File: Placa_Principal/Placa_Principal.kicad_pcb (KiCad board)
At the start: 2 copper layers, 126.7 x 163.3 mm, 23 parts, among them J1 Conn_01x02, J2 Conn_01x02, J3 Conn_01x02, J4 Conn_01x02, J5 Conn_01x02, Q1 BC547, Q2 IRF9540N, SW1 MTS102-C4, U1 LM358, U2 ESP32-S3-DevKitC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

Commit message: Segundo commit
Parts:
- added C2: 100uF, Capacitor_THT:CP_Radial_D8.0mm_P3.50mm, F.Cu at (53.9, 85.6)
- added R5: 330, Resistor_THT:R_Axial_DIN0204_L3.6mm_D1.6mm_P5.08mm_Horizontal, F.Cu at (70.4, 146.4)
- added U7: 4N25, Package_DIP:DIP-8_W7.62mm_Socket, F.Cu at (67.2, 121.8)
- D1: footprint LED_THT:LED_D4.0mm -> LED_THT:LED_D10.0mm
- moved J2 35.7 mm to (99.3, 84.9), turned to 180 degrees
- moved Q2 30.3 mm to (131.1, 153.7)
- moved J3 21.7 mm to (92.2, 84.9), turned to 180 degrees
- moved J1 20.0 mm to (106.9, 157.9)
- moved R4 17.6 mm to (95.4, 124.6)
- moved D1 13.3 mm to (96.4, 135.5)
- moved SW1 12.7 mm to (81.3, 162.2)
- moved J5 9.07 mm to (77.9, 84.9), turned to 180 degrees
- moved J4 8.54 mm to (85.0, 84.9), turned to 180 degrees
- moved U4 6.58 mm to (136.2, 71.9), turned to 0 degrees
- moved U3 4.14 mm to (88.6, 143.3), turned to 90 degrees
- moved U6 3.22 mm to (110.3, 73.0)
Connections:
- J2 pad 1: Net-(J2-Pin_1) -> ESP_GPIO04
- J2 pad 2: Net-(J2-Pin_2) -> ESP_GPIO05
- J3 pad 1: Net-(J3-Pin_1) -> ESP_GPIO06
- J3 pad 2: Net-(J3-Pin_2) -> ESP_GPIO07
- J4 pad 1: Net-(J4-Pin_1) -> ESP_GPIO15
- J4 pad 2: Net-(J4-Pin_2) -> ESP_GPIO16
- J5 pad 1: Net-(J5-Pin_1) -> ESP_GPIO17
- J5 pad 2: Net-(J5-Pin_2) -> ESP_GPIO18
- U2 pad 10: unconnected-(U2-GPIO17/ADC2_CH6-Pad10) -> ESP_GPIO17
- U2 pad 11: unconnected-(U2-GPIO18/ADC2_CH7-Pad11) -> ESP_GPIO18
- U2 pad 12: unconnected-(U2-GPIO8/ADC1_CH7-Pad12) -> ESP_GPIO08
- U2 pad 13: unconnected-(U2-GPIO3/ADC1_CH2-Pad13) -> ESP_GPIO03
- U2 pad 14: unconnected-(U2-GPIO46-Pad14) -> ESP_GPIO46
- U2 pad 15: unconnected-(U2-GPIO9/ADC1_CH8-Pad15) -> ESP_GPIO09
- U2 pad 16: unconnected-(U2-GPIO10/ADC1_CH9-Pad16) -> SPI
- U2 pad 17: unconnected-(U2-GPIO11/ADC2_CH0-Pad17) -> SPI
- U2 pad 18: unconnected-(U2-GPIO12/ADC2_CH1-Pad18) -> SPI
- U2 pad 19: unconnected-(U2-GPIO13/ADC2_CH2-Pad19) -> SPI
- U2 pad 20: unconnected-(U2-GPIO14/ADC2_CH3-Pad20) -> ESP_GPIO14
- U2 pad 30: unconnected-(U2-GPIO45-Pad30) -> ESP_GPIO45
- U2 pad 4: unconnected-(U2-GPIO4/ADC1_CH3-Pad4) -> ESP_GPIO04
- U2 pad 5: unconnected-(U2-GPIO5/ADC1_CH4-Pad5) -> ESP_GPIO05
- U2 pad 6: unconnected-(U2-GPIO6/ADC1_CH5-Pad6) -> ESP_GPIO06
- U2 pad 7: unconnected-(U2-GPIO7/ADC1_CH6-Pad7) -> ESP_GPIO07
- U2 pad 8: unconnected-(U2-GPIO15/ADC2_CH4/32K_P-Pad8) -> ESP_GPIO15
- U2 pad 9: unconnected-(U2-GPIO16/ADC2_CH5/32K_N-Pad9) -> ESP_GPIO16
- U4 pad 1: Net-(J3-Pin_2) -> unconnected-(U4-IN1L-Pad1)
- U4 pad 2: Net-(J3-Pin_1) -> unconnected-(U4-IN2L-Pad2)
- U4 pad 3: Net-(J2-Pin_2) -> unconnected-(U4-IN3L-Pad3)
- U4 pad 4: Net-(J2-Pin_1) -> unconnected-(U4-IN4L-Pad4)
- U5 pad 1: Net-(J5-Pin_2) -> unconnected-(U5-IN1L-Pad1)
- U5 pad 2: Net-(J5-Pin_1) -> unconnected-(U5-IN2L-Pad2)
- U5 pad 3: Net-(J4-Pin_2) -> unconnected-(U5-IN3L-Pad3)
- U5 pad 4: Net-(J4-Pin_1) -> unconnected-(U5-IN4L-Pad4)
- U6 pad 1: unconnected-(U6-VCC-Pad1) -> +3.3V
- U6 pad 2: unconnected-(U6-GND-Pad2) -> GND
- U6 pad 3: unconnected-(U6-SCL/SCLK-Pad3) -> ESP_GPIO09
- U6 pad 4: unconnected-(U6-SDA/SDI-Pad4) -> ESP_GPIO08
- U6 pad 7: unconnected-(U6-AD0/SDO-Pad7) -> ESP_GPIO46
- U6 pad 8: unconnected-(U6-INT-Pad8) -> ESP_GPIO03
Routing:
- net VCC: track 0.00 -> 48.5 mm
- net GND: track 63.4 -> 111.9 mm

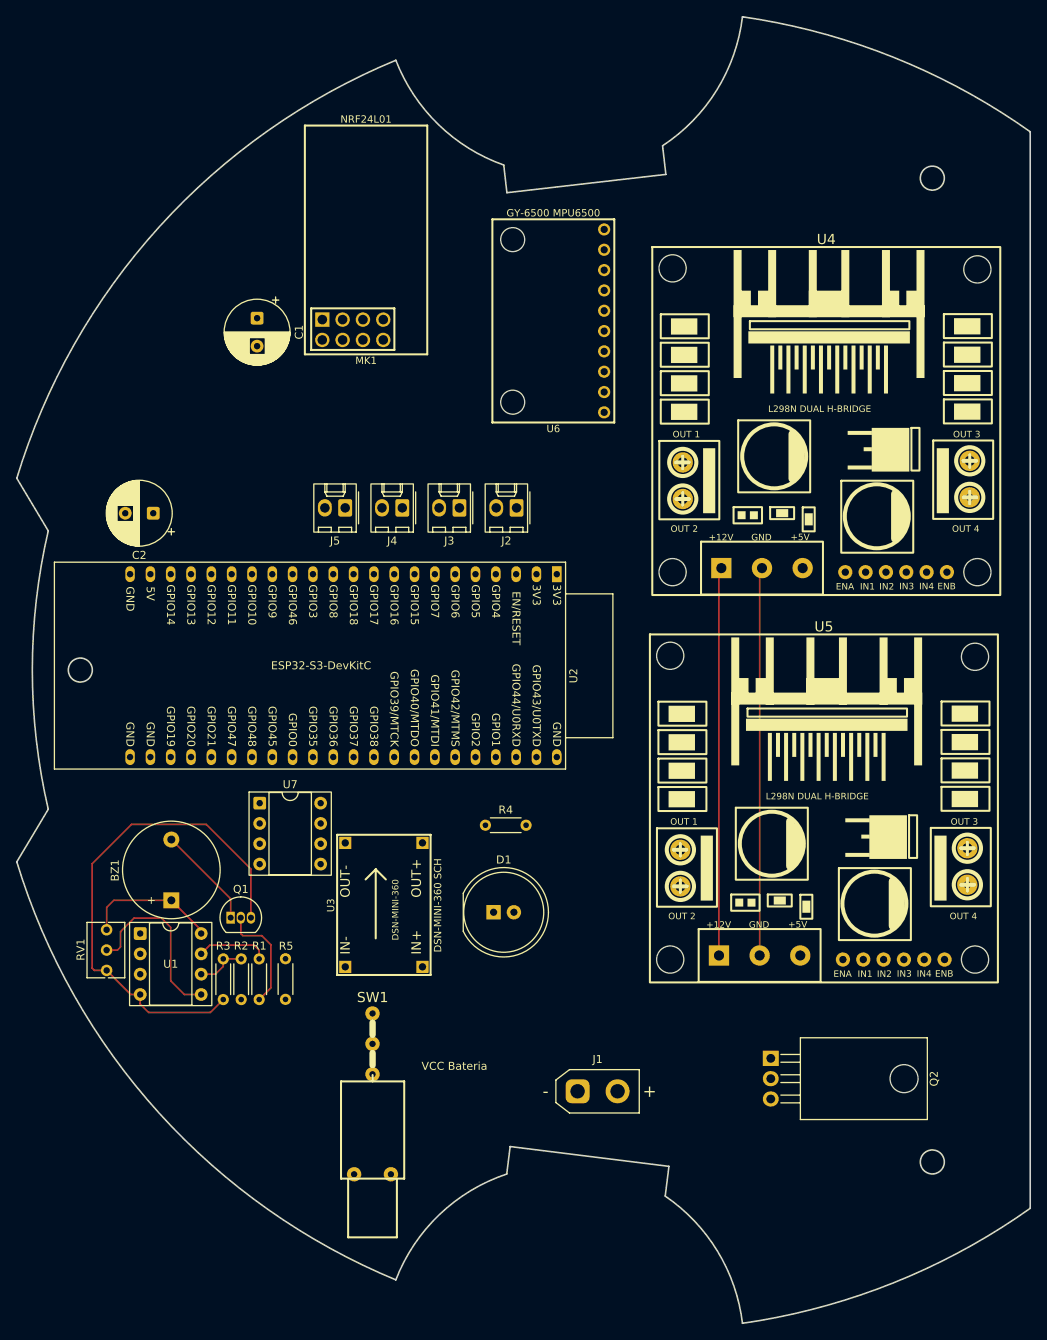
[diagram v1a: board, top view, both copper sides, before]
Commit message: Finalizando o esquemático e rearranjando a posição dos componentes na PCB
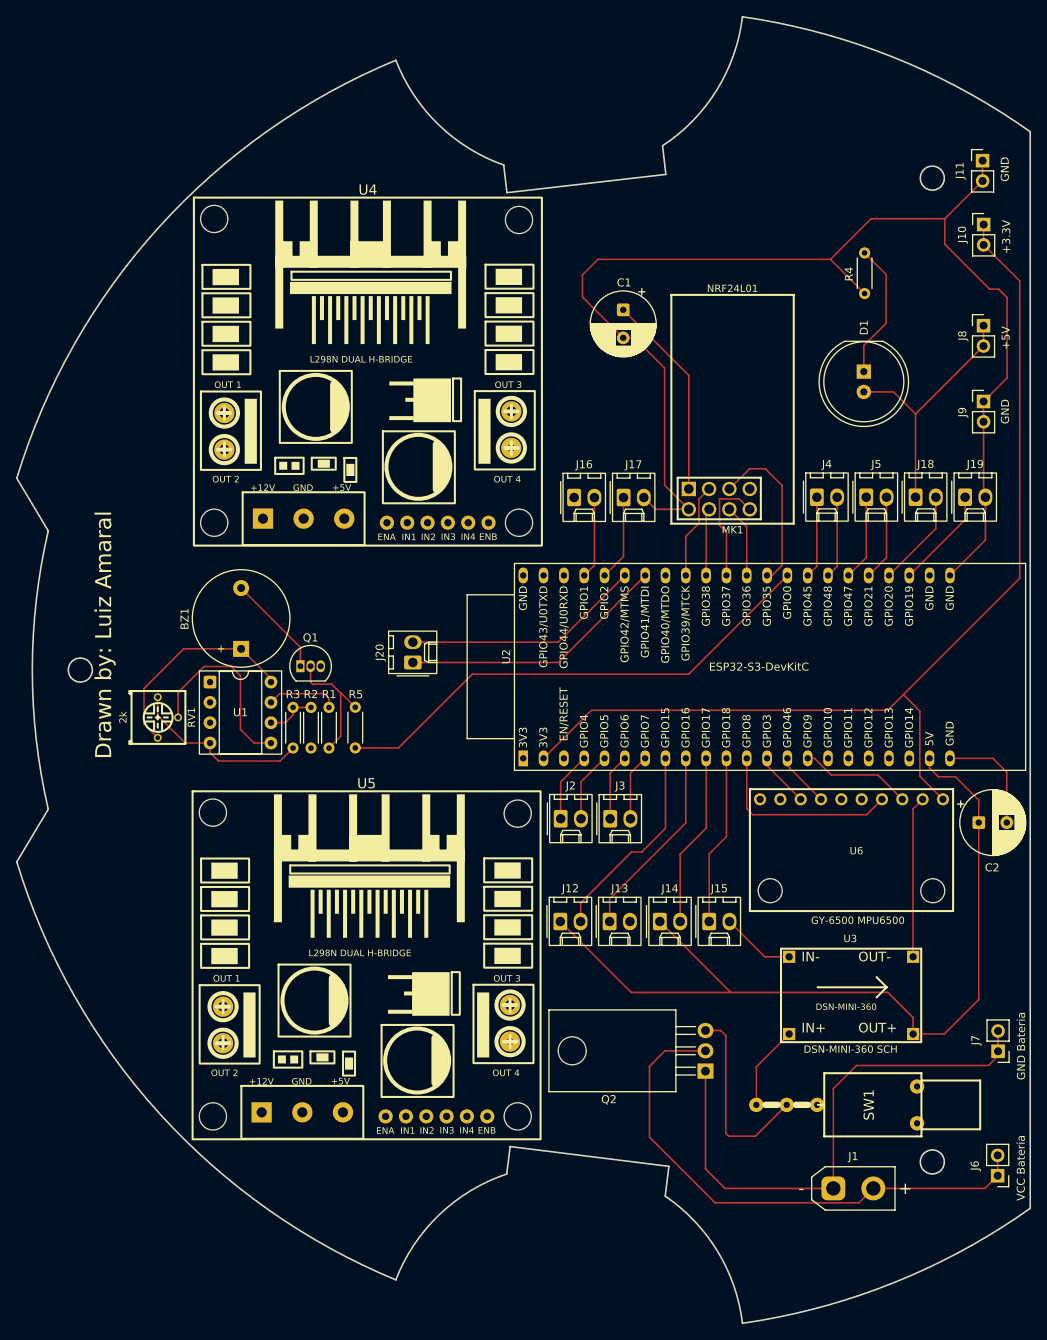
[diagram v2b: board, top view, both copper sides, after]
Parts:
- removed U7: 4N25, Package_DIP:DIP-8_W7.62mm_Socket
- added J10: Conn_01x02_Pin, Connector_PinHeader_2.54mm:PinHeader_1x02_P2.54mm_Vertical, F.Cu at (157.7, 49.5)
- added J11: Conn_01x02_Pin, Connector_PinHeader_2.54mm:PinHeader_1x02_P2.54mm_Vertical, F.Cu at (157.6, 41.5)
- added J12: Conn_01x02, Connector_Molex:Molex_KK-254_AE-6410-02A_1x02_P2.54mm_Vertical, F.Cu at (104.8, 136.6)
- added J13: Conn_01x02, Connector_Molex:Molex_KK-254_AE-6410-02A_1x02_P2.54mm_Vertical, F.Cu at (110.9, 136.6)
- added J14: Conn_01x02, Connector_Molex:Molex_KK-254_AE-6410-02A_1x02_P2.54mm_Vertical, F.Cu at (117.2, 136.6)
- added J15: Conn_01x02, Connector_Molex:Molex_KK-254_AE-6410-02A_1x02_P2.54mm_Vertical, F.Cu at (123.4, 136.6)
- added J16: Conn_01x02, Connector_Molex:Molex_KK-254_AE-6410-02A_1x02_P2.54mm_Vertical, F.Cu at (106.5, 83.6)
- added J17: Conn_01x02, Connector_Molex:Molex_KK-254_AE-6410-02A_1x02_P2.54mm_Vertical, F.Cu at (112.7, 83.6)
- added J18: Conn_01x02, Connector_Molex:Molex_KK-254_AE-6410-02A_1x02_P2.54mm_Vertical, F.Cu at (149.2, 83.6)
- added J19: Conn_01x02, Connector_Molex:Molex_KK-254_AE-6410-02A_1x02_P2.54mm_Vertical, F.Cu at (155.4, 83.6)
- added J20: Conn_01x02, Connector_Molex:Molex_KK-254_AE-6410-02A_1x02_P2.54mm_Vertical, F.Cu at (86.3, 104.3)
- added J6: Conn_01x02_Pin, Connector_PinHeader_2.54mm:PinHeader_1x02_P2.54mm_Vertical, F.Cu at (159.4, 168.4)
- added J7: Conn_01x02_Pin, Connector_PinHeader_2.54mm:PinHeader_1x02_P2.54mm_Vertical, F.Cu at (159.5, 152.9)
- added J8: Conn_01x02_Pin, Connector_PinHeader_2.54mm:PinHeader_1x02_P2.54mm_Vertical, F.Cu at (157.7, 62.2)
- added J9: Conn_01x02_Pin, Connector_PinHeader_2.54mm:PinHeader_1x02_P2.54mm_Vertical, F.Cu at (157.7, 71.6)
- R5: value 330 -> ?
- RV1: value R_Potentiometer -> 2k; footprint Potentiometer_THT:Potentiometer_Bourns_3266Y_Vertical -> Custom_Footprints:RTRIM3362P
- moved C2 110.2 mm to (157.1, 124.3), turned to 0 degrees
- moved R4 85.8 mm to (142.8, 53.1), turned to -90 degrees
- moved D1 81.9 mm to (142.7, 67.9), turned to -90 degrees
- moved J5 65.1 mm to (143.0, 83.6), turned to 0 degrees
- moved U6 64.3 mm to (152.6, 121.4), turned to -90 degrees
- moved SW1 62.1 mm to (143.4, 159.6), turned to 90 degrees
- moved U5 60.4 mm to (78.8, 139.9)
- moved U4 57.6 mm to (78.9, 65.7)
- moved J4 51.8 mm to (136.8, 83.6), turned to 0 degrees
- moved MK1 50.5 mm to (124.7, 83.8)
- moved C1 45.8 mm to (112.6, 60.2)
- moved U3 44.6 mm to (132.4, 151.7), turned to 0 degrees
- moved J3 43.2 mm to (111.0, 123.8), turned to 0 degrees
- moved J2 39.3 mm to (104.8, 123.8), turned to 0 degrees
- moved J1 34.2 mm to (138.9, 170.0)
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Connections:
- J4 pad 1: ESP_GPIO15 -> ESP_GPIO45
- J4 pad 2: ESP_GPIO16 -> ESP_GPIO48
- J5 pad 1: ESP_GPIO17 -> ESP_GPIO47
- J5 pad 2: ESP_GPIO18 -> ESP_GPIO21
- R5 pad 1: ESP_GPIO14 -> ESP_GPIO00
- U2 pad 16: SPI -> SPI_CS
- U2 pad 17: SPI -> SPI_MOSI
- U2 pad 18: SPI -> SPI_CLK
- U2 pad 19: SPI -> SPI_MISO
- U2 pad 20: ESP_GPIO14 -> unconnected-(U2-GPIO14/ADC2_CH3-Pad20)
- U2 pad 25: unconnected-(U2-GPIO19/USB_D--Pad25) -> ESP_GPIO19
- U2 pad 26: unconnected-(U2-GPIO20/USB_D+-Pad26) -> ESP_GPIO20
- U2 pad 27: unconnected-(U2-GPIO21-Pad27) -> ESP_GPIO21
- U2 pad 28: unconnected-(U2-GPIO47-Pad28) -> ESP_GPIO47
- U2 pad 29: unconnected-(U2-GPIO48-Pad29) -> ESP_GPIO48
- U2 pad 31: unconnected-(U2-GPIO0-Pad31) -> ESP_GPIO00
- U2 pad 38: unconnected-(U2-GPIO41/MTDI-Pad38) -> ESP_GPIO41
- U2 pad 39: unconnected-(U2-GPIO42/MTMS-Pad39) -> ESP_GPIO42
- U2 pad 40: unconnected-(U2-GPIO2/ADC1_CH1-Pad40) -> ESP_GPIO02
- U2 pad 41: unconnected-(U2-GPIO1/ADC1_CH0-Pad41) -> ESP_GPIO01
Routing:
- net GND: track 111.9 -> 290.5 mm
- net +3.3V: track 0.00 -> 155.8 mm
- net +5V: track 17.0 -> 167.0 mm
- net ESP_GPIO00: track 0.00 -> 62.9 mm
- net ESP_GPIO41: track 0.00 -> 33.5 mm
- net ESP_GPIO42: track 0.00 -> 30.0 mm
- net ESP_GPIO15: track 0.00 -> 25.5 mm
- net Net-(Q2-S): track 0.00 -> 24.4 mm
- net ESP_GPIO16: track 0.00 -> 24.3 mm
- net ESP_GPIO08: track 0.00 -> 24.3 mm
- net ESP_GPIO17: track 0.00 -> 21.7 mm
- net ESP_GPIO18: track 0.00 -> 21.3 mm
- net ESP_GPIO35: track 0.00 -> 20.9 mm
- net VCC: track 48.5 -> 67.5 mm
- net Net-(D1-K): track 0.00 -> 17.1 mm
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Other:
- board text added: "+3.3V"
- board text added: "+5V"
- board text added: "Drawn by: Luiz Amaral"
- board text added: "GND"
- board text added: "GND Bateria"

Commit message: Atualizando a alimentação de todos os sensores e ESP para 3.3V e finalizando o design do monitoramento da bateria e feedback geral
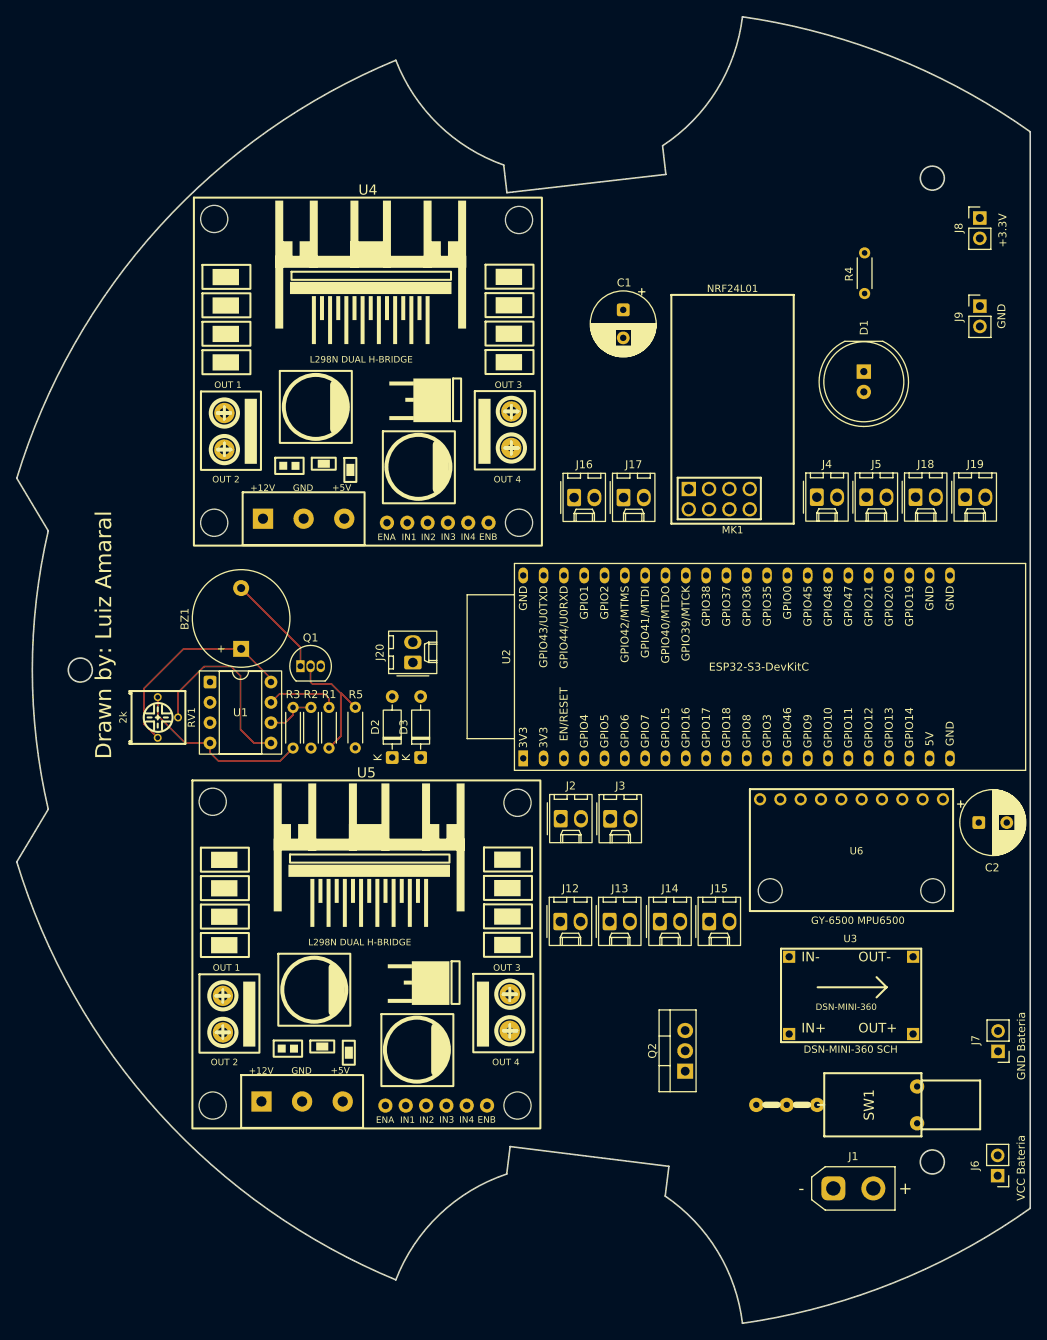
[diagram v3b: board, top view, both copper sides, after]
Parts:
- removed J10, J11: Conn_01x02_Pin, Connector_PinHeader_2.54mm:PinHeader_1x02_P2.54mm_Vertical
- added D2: 1N4148, Diode_THT:D_DO-35_SOD27_P7.62mm_Horizontal, F.Cu at (83.8, 116.1)
- added D3: 1N4148, Diode_THT:D_DO-35_SOD27_P7.62mm_Horizontal, F.Cu at (87.3, 116.1)
- Q2: footprint Package_TO_SOT_THT:TO-220-3_Horizontal_TabDown -> Package_TO_SOT_THT:TO-220-3_Vertical
- R2: value R_Small_US -> 47k
- R3: value R_Small_US -> 12k
- R5: value ? -> 1k
- moved J8 13.5 mm to (157.2, 48.7)
- moved J9 11.9 mm to (157.2, 59.7)
- moved Q2 2.54 mm to (120.4, 155.3)
- moved U5 1.36 mm to (78.7, 138.6)
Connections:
- BZ1 pad 1: +5V -> +3.3V
- C2 pad 1: +5V -> +3.3V
- D1 pad 2: +5V -> +3.3V
- J12 pad 1: +5V -> +3.3V
- J14 pad 1: +5V -> +3.3V
- J16 pad 1: +5V -> +3.3V
- J18 pad 1: +5V -> +3.3V
- J8 pad 1: +5V -> +3.3V
- J8 pad 2: +5V -> +3.3V
- Q1 pad 2: Net-(Q1-B) -> Net-(D2-K)
- R1 pad 2: Net-(Q1-B) -> Net-(D3-A)
- R5 pad 2: Net-(Q1-B) -> Net-(D2-A)
- RV1 pad 3: +5V -> +3.3V
- U1 pad 8: +5V -> +3.3V
- U2 pad 21: +5V -> unconnected-(U2-5V-Pad21)
- U3 pad 3: +5V -> +3.3V
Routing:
- net GND: track 290.5 -> 22.9 mm
- net +5V: track 167.0 -> 0.00 mm
- net +3.3V: track 155.8 -> 26.8 mm
- net VCC: track 67.5 -> 0.00 mm
- net ESP_GPIO00: track 62.9 -> 0.00 mm
- net ESP_GPIO41: track 33.5 -> 0.00 mm
- net ESP_GPIO42: track 30.0 -> 0.00 mm
- net ESP_GPIO15: track 25.5 -> 0.00 mm
- net Net-(Q2-S): track 24.4 -> 0.00 mm
- net ESP_GPIO16: track 24.3 -> 0.00 mm
- net ESP_GPIO08: track 24.3 -> 0.00 mm
- net ESP_GPIO17: track 21.7 -> 0.00 mm
- net ESP_GPIO18: track 21.3 -> 0.00 mm
- net ESP_GPIO35: track 20.9 -> 0.00 mm
- net Net-(D1-K): track 17.1 -> 0.00 mm
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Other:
- board text removed: "+5V"
